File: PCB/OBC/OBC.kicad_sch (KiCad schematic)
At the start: 1 part

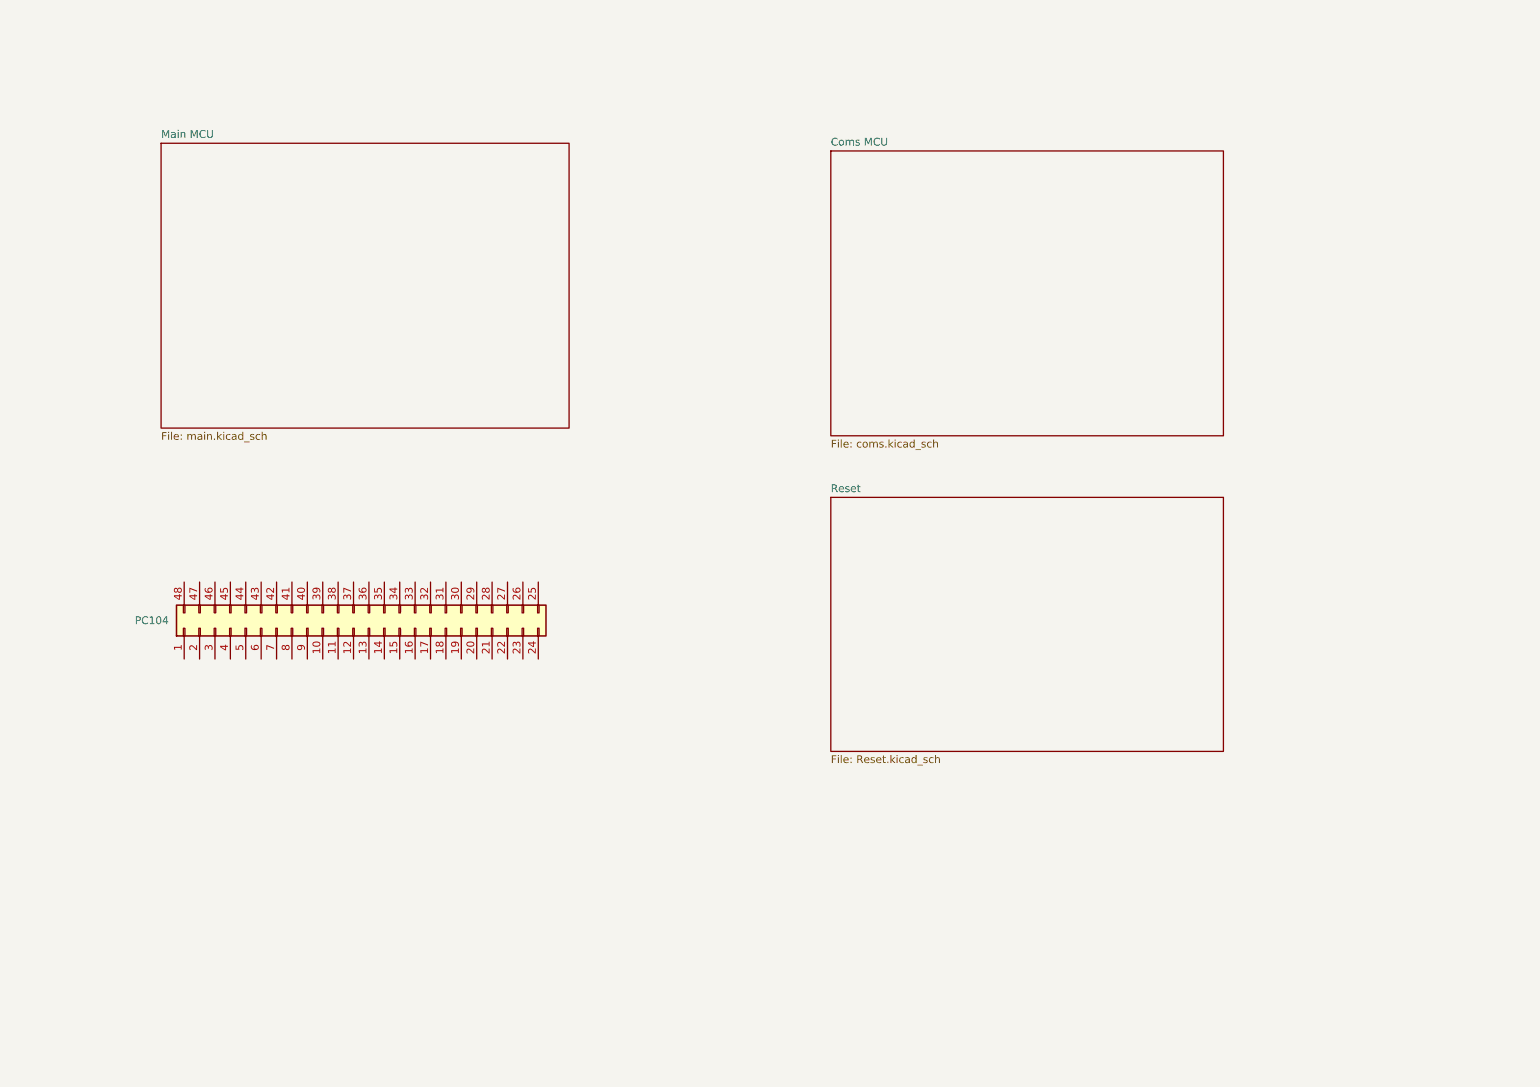
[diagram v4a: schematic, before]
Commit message: Add: flash memory and mux at libraries
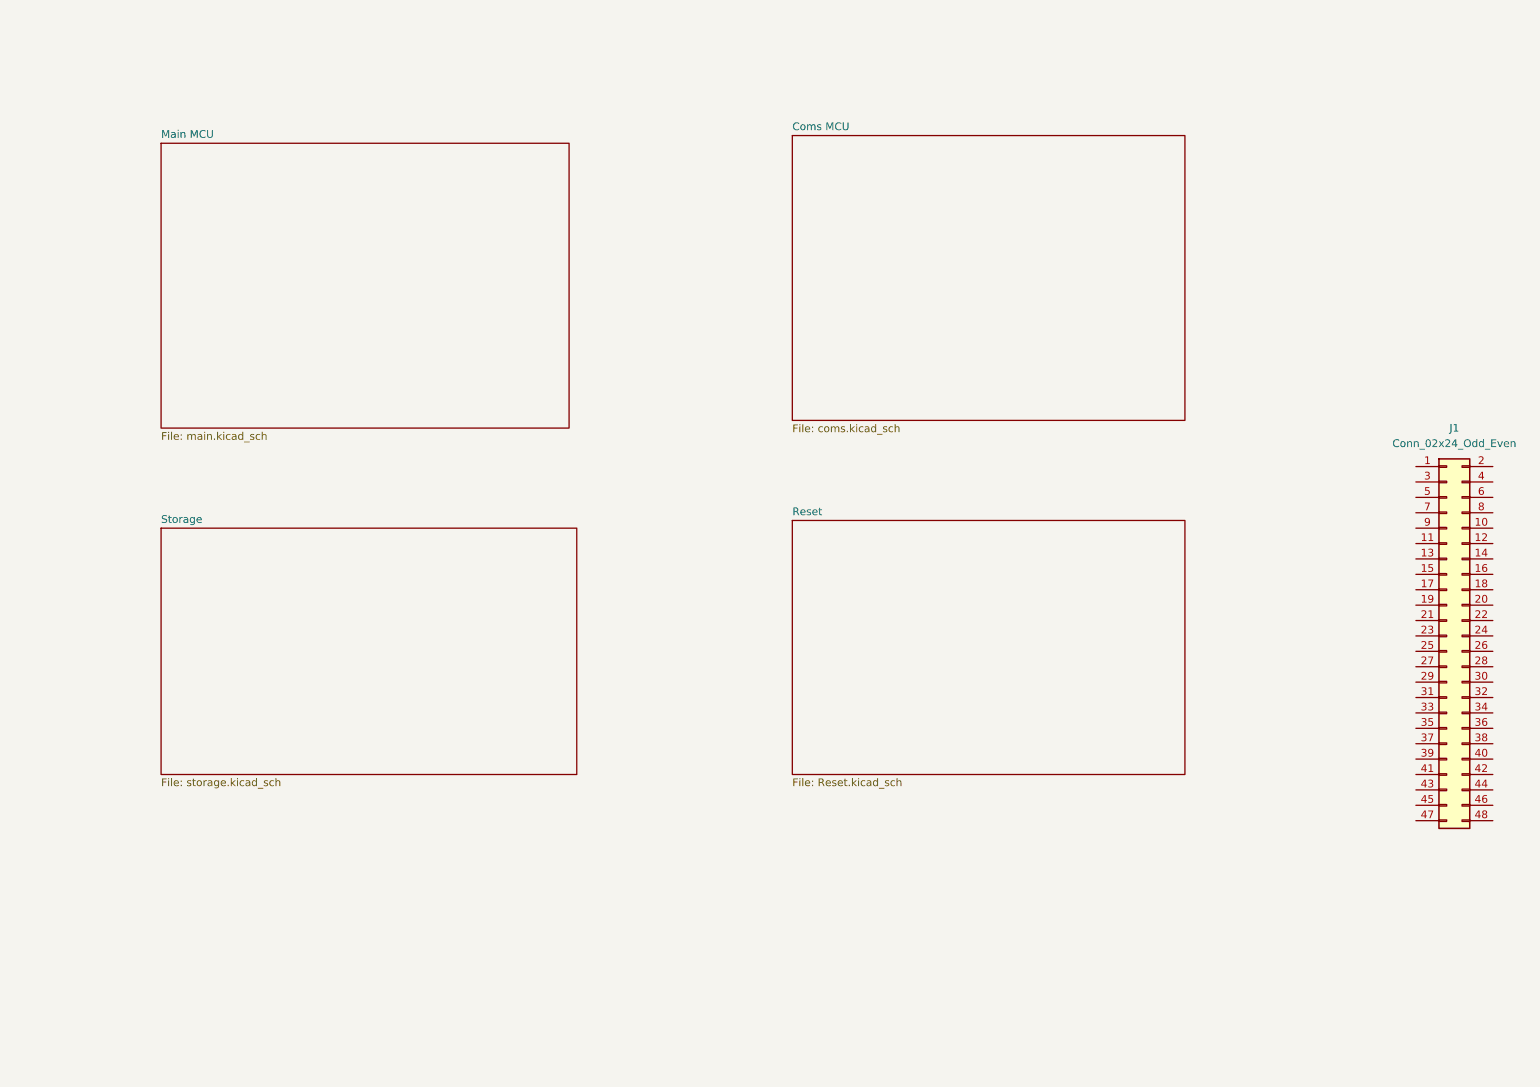
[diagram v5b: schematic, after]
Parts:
- removed PC104: Conn_02x24_Counter_Clockwise, Connector_PinHeader_2.54mm:PinHeader_2x24_P2.54mm_Vertical, symbol Connector_Generic:Conn_02x24_Counter_Clockwise
- added J1: Conn_02x24_Odd_Even, symbol Connector_Generic:Conn_02x24_Odd_Even
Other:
- added sheet Storage (storage.kicad_sch)
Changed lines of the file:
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@@
 	(paper "A4")
 	(symbol
-		(lib_id "Connector_Generic:Conn_02x24_Counter_Clockwise")
-		(at 72.39 116.84 90)
+		(lib_id "Connector_Generic:Conn_02x24_Odd_Even")
+		(at 252.73 118.11 0)
 		(unit 1)
 		(exclude_from_sim no)
@@
 		(dnp no)
 		(fields_autoplaced yes)
-		(property "Reference" "PC104"
-			(at 41.91 115.5699 90)
-			(effects
-				(font
-					(size 1.27 1.27)
-				)
-				(justify left)
-			)
-		)
-		(property "Value" "Conn_02x24_Counter_Clockwise"
-			(at 40.64 115.57 0)
+		(property "Reference" "J1"
+			(at 254 83.82 0)
+			(effects
+				(font
+					(size 1.27 1.27)
+				)
+			)
+		)
+		(property "Value" "Conn_02x24_Odd_Even"
+			(at 254 86.36 0)
+			(effects
+				(font
+					(size 1.27 1.27)
+				)
+			)
+		)
+		(property "Footprint" ""
+			(at 252.73 118.11 0)
 			(effects
 				(font
@@
 			)
 		)
-		(property "Footprint" "Connector_PinHeader_2.54mm:PinHeader_2x24_P2.54mm_Vertical"
-			(at 72.39 116.84 0)
+		(property "Datasheet" "~"
+			(at 252.73 118.11 0)
 			(effects
 				(font
@@
 			)
 		)
-		(property "Datasheet" "~"
-			(at 72.39 116.84 0)
+		(property "Description" "Generic connector, double row, 02x24, odd/even pin numbering scheme (row 1 odd numbers, row 2 even numbers), script generated (kicad-library-utils/schlib/autogen/connector/)"
+			(at 252.73 118.11 0)
 			(effects
 				(font
@@
 			)
 		)
-		(property "Description" "Generic connector, double row, 02x24, counter clockwise pin numbering scheme (similar to DIP package numbering), script generated (kicad-library-utils/schlib/autogen/connector/)"
-			(at 72.39 116.84 0)
-			(effects
-				(font
-					(size 1.27 1.27)
-				)
-				(hide yes)
-			)
+		(pin "6"
+		)
+		(pin "48"
+		)
+		(pin "2"
+		)
+		(pin "4"
+		)
+		(pin "38"
+		)
+		(pin "22"
+		)
+		(pin "24"
+		)
+		(pin "44"
+		)
+		(pin "42"
+		)
+		(pin "19"
+		)
+		(pin "40"
+		)
+		(pin "46"
+		)
+		(pin "41"
+		)
+		(pin "27"
+		)
+		(pin "25"
+		)
+		(pin "30"
+		)
+		(pin "18"
+		)
+		(pin "33"
+		)
+		(pin "14"
+		)
+		(pin "15"
+		)
+		(pin "29"
+		)
+		(pin "26"
+		)
+		(pin "10"
+		)
+		(pin "36"
+		)
+		(pin "12"
+		)
+		(pin "11"
+		)
+		(pin "28"
+		)
+		(pin "34"
+		)
+		(pin "9"
+		)
+		(pin "7"
+		)
+		(pin "3"
+		)
+		(pin "5"
+		)
+		(pin "32"
+		)
+		(pin "13"
+		)
+		(pin "47"
+		)
+		(pin "43"
+		)
+		(pin "8"
+		)
+		(pin "16"
+		)
+		(pin "31"
+		)
+		(pin "37"
+		)
+		(pin "23"
+		)
+		(pin "21"
+		)
+		(pin "45"
+		)
+		(pin "17"
+		)
+		(pin "39"
+		)
+		(pin "1"
 		)
 		(pin "20"
 		)
-		(pin "34"
-		)
-		(pin "30"
-		)
-		(pin "31"
-		)
-		(pin "32"
-		)
-		(pin "23"
-		)
-		(pin "9"
-		)
-		(pin "11"
-		)
 		(pin "35"
 		)
-		(pin "33"
-		)
-		(pin "36"
-		)
-		(pin "45"
-		)
-		(pin "44"
-		)
-		(pin "47"
-		)
-		(pin "16"
-		)
-		(pin "26"
-		)
-		(pin "21"
-		)
-		(pin "22"
-		)
-		(pin "2"
-		)
-		(pin "1"
-		)
-		(pin "10"
-		)
-		(pin "40"
-		)
-		(pin "13"
-		)
-		(pin "39"
-		)
-		(pin "29"
-		)
-		(pin "43"
-		)
-		(pin "8"
-		)
-		(pin "5"
-		)
-		(pin "6"
-		)
-		(pin "7"
-		)
-		(pin "25"
-		)
-		(pin "41"
-		)
-		(pin "12"
-		)
-		(pin "42"
-		)
-		(pin "3"
-		)
-		(pin "24"
-		)
-		(pin "27"
-		)
-		(pin "15"
-		)
-		(pin "14"
-		)
-		(pin "37"
-		)
-		(pin "38"
-		)
-		(pin "19"
-		)
-		(pin "48"
-		)
-		(pin "18"
-		)
-		(pin "28"
-		)
-		(pin "17"
-		)
-		(pin "46"
-		)
-		(pin "4"
-		)
-		(instances
-			(project "OBC"
-				(path "/e2c03eef-3b12-44a7-ba52-633d5337a24a"
-					(reference "PC104")
+		(instances
+			(project "OBC"
+				(path "/e2c03eef-3b12-44a7-ba52-633d5337a24a"
+					(reference "J1")
 					(unit 1)
 				)
@@
 	)
 	(sheet
-		(at 151.13 38.1)
+		(at 144.78 35.56)
 		(size 64.77 46.99)
 		(exclude_from_sim no)
@@
 		)
 		(property "Sheetname" "Coms MCU"
-			(at 151.13 37.363 0)
+			(at 144.78 34.823 0)
 			(effects
 				(font
@@
 		)
 		(property "Sheetfile" "coms.kicad_sch"
-			(at 151.13 85.7 0)
+			(at 144.78 83.16 0)
 			(effects
 				(font
@@
 	)
 	(sheet
-		(at 151.13 95.25)
+		(at 144.78 99.06)
 		(size 64.77 41.91)
 		(exclude_from_sim no)
@@
 		)
 		(property "Sheetname" "Reset"
-			(at 151.13 94.5384 0)
+			(at 144.78 98.3484 0)
 			(effects
 				(font
@@
 		)
 		(property "Sheetfile" "Reset.kicad_sch"
-			(at 151.13 137.7446 0)
+			(at 144.78 141.5546 0)
 			(effects
 				(font
@@
 				)
 			)
+		)
+	)
+	(sheet
+		(at 40.64 100.33)
+		(size 68.58 40.64)
+		(exclude_from_sim no)
+		(in_bom yes)
+		(on_board yes)
+		(dnp no)
+		(fields_autoplaced yes)
+		(stroke
+			(width 0.1524)
+			(type solid)
+		)
+		(fill
+			(color 0 0 0 0.0000)
+		)
+		(property "Sheetname" "Storage"
+			(at 40.64 99.6184 0)
+			(effects
+				(font
+					(size 1.27 1.27)
+				)
+				(justify left bottom)
+			)
+		)
+		(property "Sheetfile" "storage.kicad_sch"
+			(at 40.64 141.5546 0)
+			(effects
+				(font
+					(size 1.27 1.27)
+				)
+				(justify left top)
+			)
+		)
+		(instances
+			(project "OBC"
+				(path "/e2c03eef-3b12-44a7-ba52-633d5337a24a"
+					(page "5")
+				)
+			)

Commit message: Watchdog
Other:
- sheet Storage renamed Power and Protections
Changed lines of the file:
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@@
 			(color 0 0 0 0.0000)
 		)
-		(property "Sheetname" "Storage"
+		(property "Sheetname" "Power and Protections"
 			(at 40.64 99.6184 0)
 			(effects

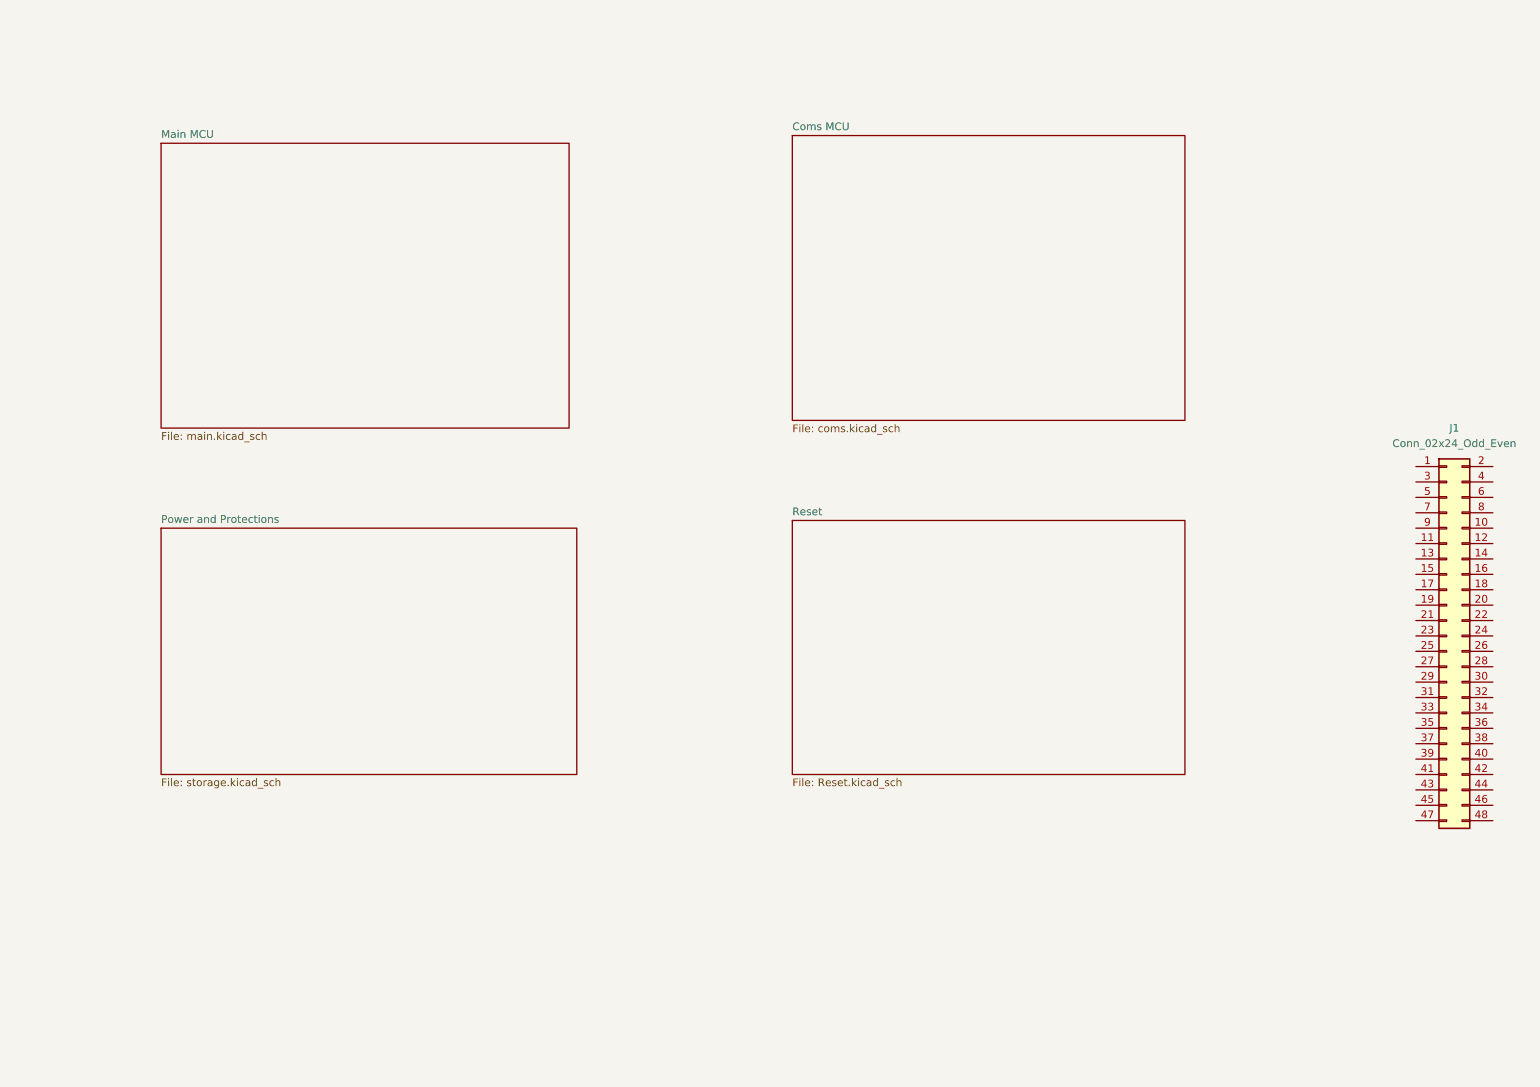
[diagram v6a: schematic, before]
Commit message: Colocacion de OCP, LDO
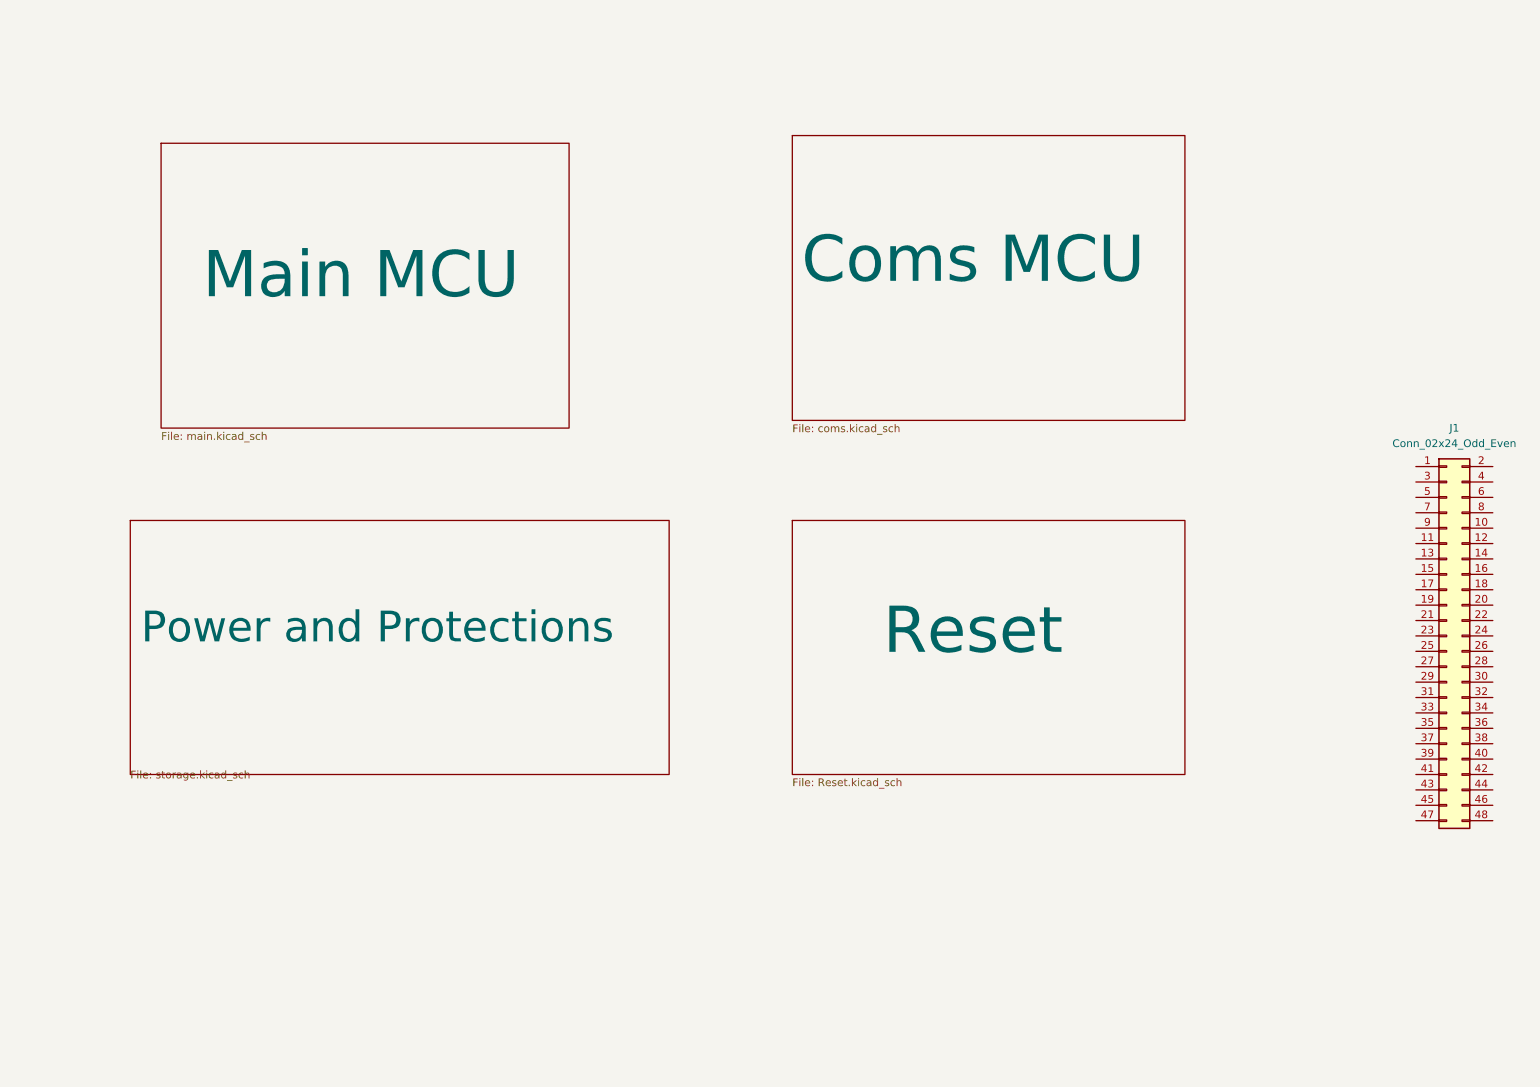
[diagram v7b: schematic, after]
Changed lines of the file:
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@@
 		(on_board yes)
 		(dnp no)
-		(fields_autoplaced yes)
 		(stroke
 			(width 0.2032)
@@
 		)
 		(property "Sheetname" "Main MCU"
-			(at 40.64 36.093 0)
+			(at 47.498 62.992 0)
 			(effects
 				(font
-					(size 1.27 1.27)
+					(size 7.62 7.62)
 				)
 				(justify left bottom)
@@
 		(on_board yes)
 		(dnp no)
-		(fields_autoplaced yes)
 		(stroke
 			(width 0.2032)
@@
 		)
 		(property "Sheetname" "Coms MCU"
-			(at 144.78 34.823 0)
+			(at 146.304 60.452 0)
 			(effects
 				(font
-					(size 1.27 1.27)
+					(size 7.62 7.62)
 				)
 				(justify left bottom)
@@
 		(on_board yes)
 		(dnp no)
-		(fields_autoplaced yes)
 		(stroke
 			(width 0.1524)
@@
 		)
 		(property "Sheetname" "Reset"
-			(at 144.78 98.3484 0)
+			(at 159.766 121.666 0)
 			(effects
 				(font
-					(size 1.27 1.27)
+					(size 7.62 7.62)
 				)
 				(justify left bottom)
@@
 	)
 	(sheet
-		(at 40.64 100.33)
-		(size 68.58 40.64)
+		(at 35.56 99.06)
+		(size 88.9 41.91)
 		(exclude_from_sim no)
 		(in_bom yes)
 		(on_board yes)
 		(dnp no)
-		(fields_autoplaced yes)
 		(stroke
 			(width 0.1524)
@@
 		)
 		(property "Sheetname" "Power and Protections"
-			(at 40.64 99.6184 0)
+			(at 37.338 119.634 0)
 			(effects
 				(font
-					(size 1.27 1.27)
+					(size 5.08 5.08)
 				)
 				(justify left bottom)
@@
 		)
 		(property "Sheetfile" "storage.kicad_sch"
-			(at 40.64 141.5546 0)
+			(at 35.56 140.2846 0)
 			(effects
 				(font
